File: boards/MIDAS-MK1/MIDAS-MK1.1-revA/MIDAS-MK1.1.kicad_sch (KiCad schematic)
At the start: 105 parts, among them J101 Left, J102 Right, J106 USB4105-GF-A, J107 DM3BT-DSF-PEJS, J108 Conn_01x02, J110 2157601003, J111 2157601003, SW101 SW_Push, SW102 SW_Push, U101 TCAL9539-Q1, U102 TCAL9539-Q1, U103 TCAL9539-Q1, U104 ESP32-S3-WROOM-1U, U105 MCP2518FDT-xSL, U106 MTFCxxxx, U107 TCAN337G, U108 ADS7138-Q1, U109 ECMF02-2AMX6, Y101 40MHz

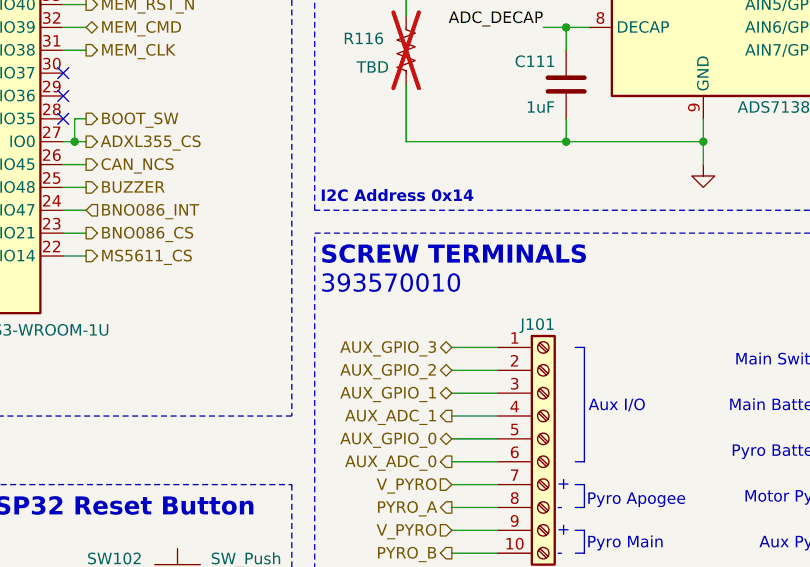
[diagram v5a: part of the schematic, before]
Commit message: rerouted regulator, added correct terminal block MPN to sch
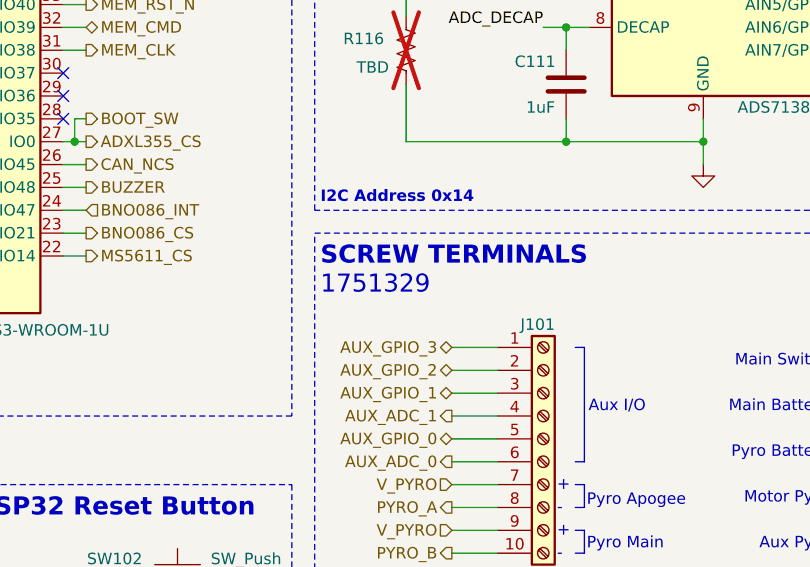
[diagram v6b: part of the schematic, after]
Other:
- note added: "1751329"
- note removed: "393570010"
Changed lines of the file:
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@@
     (effects (font (size 1.27 1.27) italic) (justify left bottom))
   )
-  (text "393570010" (at 175.895 235.585 0)
+  (text "1751329" (at 175.895 235.585 0)
     (effects (font (size 2 2)) (justify left bottom))
   )

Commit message: finalized SMA, renamed expander symbols, added backside labels, changed SYS_POWER test point, changed microSD 3D model color, other small stuff
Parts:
- U101, U102, U103: symbol Expander_Texas:TCAL9539-Q1 -> Interface_Expander_Texas:TCAL9539-Q1
- U108: symbol ADC_Texas:ADS7138-Q1 -> Analog_ADC_Texas:ADS7138-Q1
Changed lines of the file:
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@@
     )
   )
-  (symbol (lib_id "Expander_Texas:TCAL9539-Q1") (at 48.26 132.08 0) (unit 1)
+  (symbol (lib_id "Interface_Expander_Texas:TCAL9539-Q1") (at 48.26 132.08 0) (unit 1)
     (in_bom yes) (on_board yes) (dnp no)
     (property "Reference" "U102" (at 38.1 107.95 0)
@@
       (effects (font (size 1.27 1.27)) (justify left))
     )
-    (property "Footprint" "Package_DFN_QFN:WQFN-24-1EP_4x4mm_P0.5mm_EP2.6x2.6mm" (at 48.26 132.08 0)
-      (effects (font (size 1.27 1.27)) hide)
-    )
-    (property "Datasheet" "https://www.ti.com/lit/ds/symlink/tcal9539-q1.pdf" (at 48.26 132.08 0)
+    (property "Footprint" "Package_DFN_QFN:WQFN-24-1EP_4x4mm_P0.5mm_EP2.6x2.6mm" (at 48.26 162.56 0)
+      (effects (font (size 1.27 1.27)) hide)
+    )
+    (property "Datasheet" "https://www.ti.com/lit/ds/symlink/tcal9539-q1.pdf" (at 48.26 165.1 0)
       (effects (font (size 1.27 1.27)) hide)
     )
@@
     )
   )
-  (symbol (lib_name "TCAL9539-Q1_1") (lib_id "Expander_Texas:TCAL9539-Q1") (at 48.26 53.34 0) (unit 1)
+  (symbol (lib_id "Interface_Expander_Texas:TCAL9539-Q1") (at 48.26 53.34 0) (unit 1)
     (in_bom yes) (on_board yes) (dnp no)
     (property "Reference" "U101" (at 38.1 29.21 0)
@@
       (effects (font (size 1.27 1.27)) (justify left))
     )
-    (property "Footprint" "Package_DFN_QFN:WQFN-24-1EP_4x4mm_P0.5mm_EP2.6x2.6mm" (at 48.26 53.34 0)
-      (effects (font (size 1.27 1.27)) hide)
-    )
-    (property "Datasheet" "https://www.ti.com/lit/ds/symlink/tcal9539-q1.pdf" (at 48.26 53.34 0)
+    (property "Footprint" "Package_DFN_QFN:WQFN-24-1EP_4x4mm_P0.5mm_EP2.6x2.6mm" (at 48.26 83.82 0)
+      (effects (font (size 1.27 1.27)) hide)
+    )
+    (property "Datasheet" "https://www.ti.com/lit/ds/symlink/tcal9539-q1.pdf" (at 48.26 86.36 0)
       (effects (font (size 1.27 1.27)) hide)
     )
@@
     )
   )
-  (symbol (lib_id "ADC_Texas:ADS7138-Q1") (at 220.98 198.12 0) (unit 1)
+  (symbol (lib_id "Analog_ADC_Texas:ADS7138-Q1") (at 220.98 198.12 0) (unit 1)
     (in_bom yes) (on_board yes) (dnp no)
     (property "Reference" "U108" (at 208.28 184.15 0)
@@
       (effects (font (size 1.27 1.27)) (justify left))
     )
-    (property "Footprint" "Package_DFN_QFN:WQFN-16-1EP_3x3mm_P0.5mm_EP1.68x1.68mm" (at 220.98 198.12 0)
-      (effects (font (size 1.27 1.27)) hide)
-    )
-    (property "Datasheet" "https://www.ti.com/lit/ds/symlink/ads7138-q1.pdf" (at 220.98 198.12 0)
+    (property "Footprint" "Package_DFN_QFN:WQFN-16-1EP_3x3mm_P0.5mm_EP1.68x1.68mm" (at 220.98 218.44 0)
+      (effects (font (size 1.27 1.27)) hide)
+    )
+    (property "Datasheet" "https://www.ti.com/lit/ds/symlink/ads7138-q1.pdf" (at 220.98 220.98 0)
       (effects (font (size 1.27 1.27)) hide)
     )
@@
     )
   )
-  (symbol (lib_id "Expander_Texas:TCAL9539-Q1") (at 48.26 210.82 0) (unit 1)
+  (symbol (lib_id "Interface_Expander_Texas:TCAL9539-Q1") (at 48.26 210.82 0) (unit 1)
     (in_bom yes) (on_board yes) (dnp no)
     (property "Reference" "U103" (at 38.1 186.69 0)
@@
       (effects (font (size 1.27 1.27)) (justify left))
     )
-    (property "Footprint" "Package_DFN_QFN:WQFN-24-1EP_4x4mm_P0.5mm_EP2.6x2.6mm" (at 48.26 210.82 0)
-      (effects (font (size 1.27 1.27)) hide)
-    )
-    (property "Datasheet" "https://www.ti.com/lit/ds/symlink/tcal9539-q1.pdf" (at 48.26 210.82 0)
-      (effects (font (size 1.27 1.27)) hide)
-    )
+    (property "Footprint" "Package_DFN_QFN:WQFN-24-1EP_4x4mm_P0.5mm_EP2.6x2.6mm" (at 48.26 241.3 0)
+      (effects (font (size 1.27 1.27)) hide)
+    )
+    (property "Datasheet" "https://www.ti.com/lit/ds/symlink/tcal9539-q1.pdf" (at 48.26 243.84 0)
+      (effects (font (size 1.27 1.27)) hide)
+    )

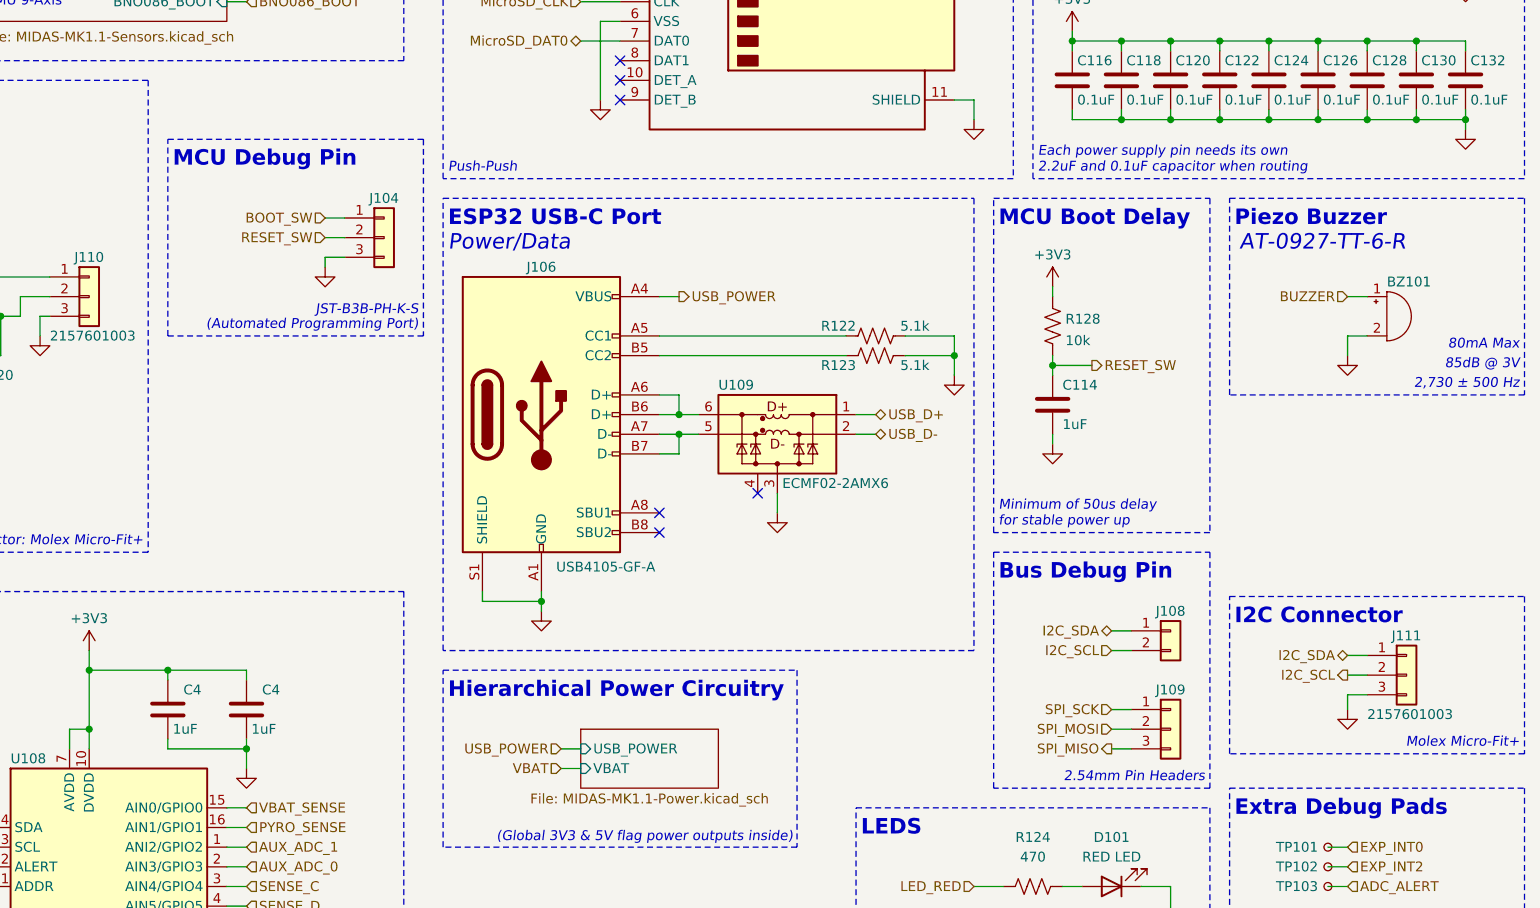
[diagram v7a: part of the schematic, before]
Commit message: schematic organizational changes
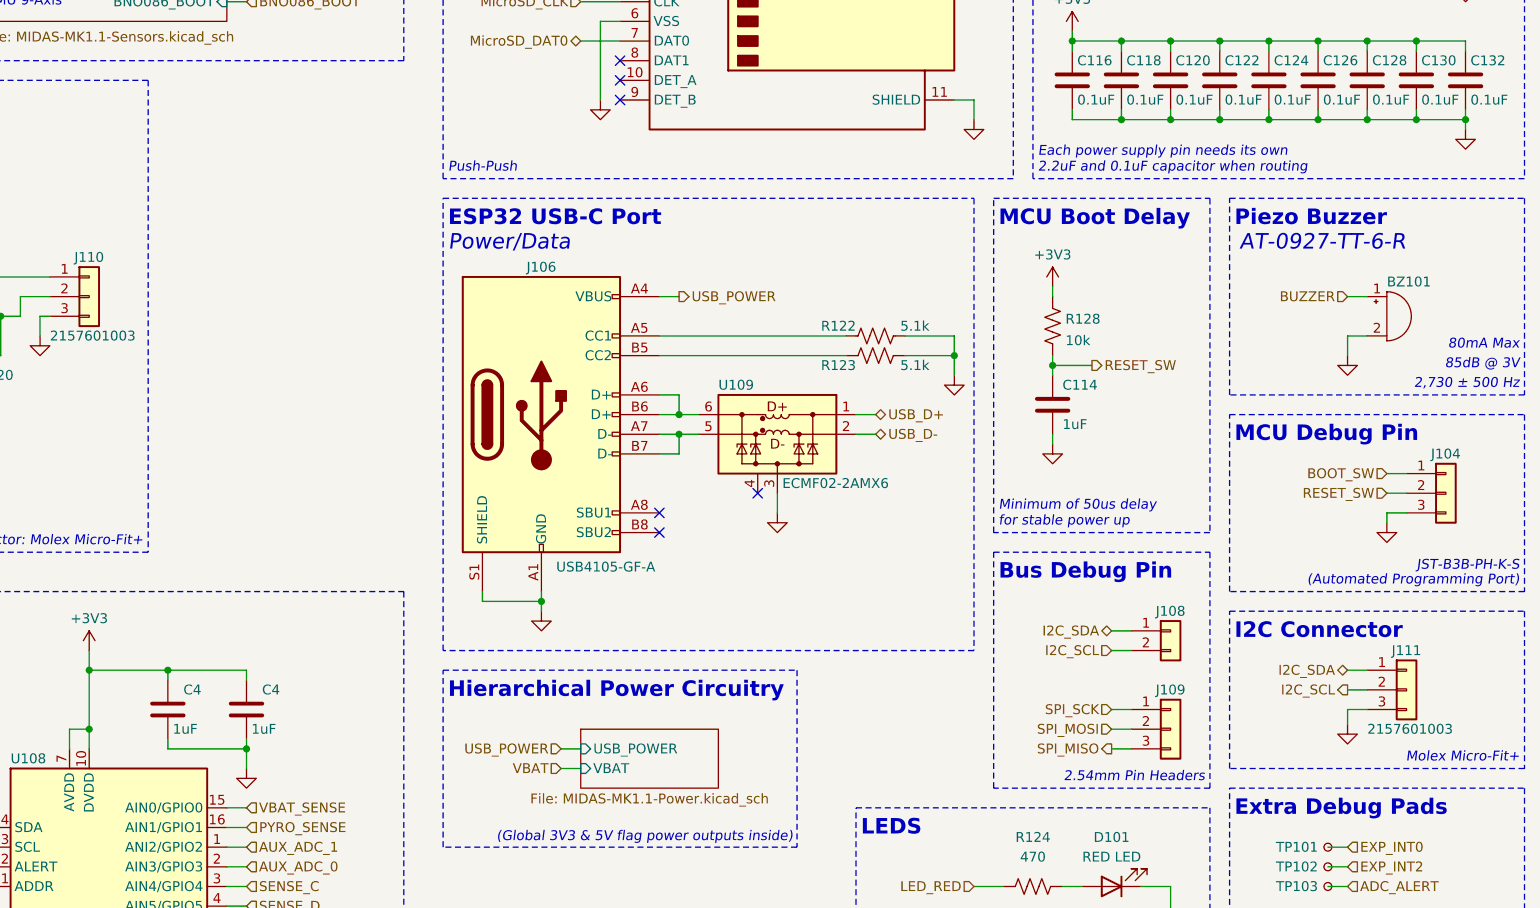
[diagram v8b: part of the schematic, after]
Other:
- moved on the sheet: J104, J111
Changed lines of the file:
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@@
     (stroke (width 0) (type default))
   )
-  (wire (pts (xy 248.92 114.3) (xy 251.46 114.3))
+  (wire (pts (xy 386.08 147.32) (xy 388.62 147.32))
     (stroke (width 0) (type default))
   )
@@
     (stroke (width 0) (type default))
   )
-  (wire (pts (xy 381 175.895) (xy 383.54 175.895))
+  (wire (pts (xy 381 177.8) (xy 383.54 177.8))
     (stroke (width 0) (type default))
   )
@@
     (stroke (width 0) (type default))
   )
-  (wire (pts (xy 381 175.895) (xy 381 177.8))
+  (wire (pts (xy 381 177.8) (xy 381 179.705))
     (stroke (width 0) (type default))
   )
@@
     (stroke (width 0) (type default))
   )
-  (wire (pts (xy 381 170.815) (xy 383.54 170.815))
+  (wire (pts (xy 381 172.72) (xy 383.54 172.72))
     (stroke (width 0) (type default))
   )
@@
     (stroke (width 0) (type default))
   )
-  (wire (pts (xy 381 173.355) (xy 383.54 173.355))
+  (wire (pts (xy 381 175.26) (xy 383.54 175.26))
     (stroke (width 0) (type default))
   )
@@
     (stroke (width 0) (type default))
   )
-  (wire (pts (xy 248.92 119.38) (xy 248.92 120.65))
+  (wire (pts (xy 386.08 152.4) (xy 386.08 153.67))
     (stroke (width 0) (type default))
   )
@@
     (stroke (width 0) (type default))
   )
-  (wire (pts (xy 248.92 116.84) (xy 251.46 116.84))
+  (wire (pts (xy 386.08 149.86) (xy 388.62 149.86))
     (stroke (width 0) (type default))
   )
@@
     (stroke (width 0) (type default))
   )
-  (wire (pts (xy 251.46 119.38) (xy 248.92 119.38))
+  (wire (pts (xy 388.62 152.4) (xy 386.08 152.4))
     (stroke (width 0) (type default))
   )
@@
     (stroke (width 0) (type default))
   )
-  (rectangle (start 228.6 104.14) (end 261.62 129.54)
+  (rectangle (start 365.76 139.7) (end 403.86 162.56)
     (stroke (width 0) (type dash))
     (fill (type none))
@@
     (fill (type none))
   )
-  (rectangle (start 365.76 163.195) (end 403.86 183.515)
+  (rectangle (start 365.76 165.1) (end 403.86 185.42)
     (stroke (width 0) (type dash))
     (fill (type none))
@@
     (effects (font (size 1.27 1.27) italic) (justify left bottom))
   )
-  (text "MCU Debug Pin\n\n" (at 229.235 111.125 0)
+  (text "MCU Debug Pin\n\n" (at 366.395 146.685 0)
     (effects (font (size 2 2) (thickness 0.4) bold) (justify left bottom))
   )
@@
     (effects (font (size 2 2) (thickness 0.4) bold) (justify left bottom))
   )
-  (text "(Automated Programming Port)" (at 260.985 128.905 0)
+  (text "(Automated Programming Port)" (at 403.225 161.925 0)
     (effects (font (size 1.27 1.27) italic) (justify right bottom))
   )
@@
     (effects (font (size 1.27 1.27)) (justify left bottom))
   )
-  (text "Molex Micro-Fit+" (at 403.225 182.88 0)
+  (text "Molex Micro-Fit+" (at 403.225 184.785 0)
     (effects (font (size 1.27 1.27) italic) (justify right bottom))
   )
@@
     (effects (font (size 1.27 1.27)) (justify left bottom))
   )
-  (text "JST-B3B-PH-K-S" (at 260.985 127 0)
+  (text "JST-B3B-PH-K-S" (at 403.225 160.02 0)
     (effects (font (size 1.27 1.27) italic) (justify right bottom))
   )
@@
     (effects (font (size 1.27 1.27)) (justify left bottom))
   )
-  (text "I2C Connector\n" (at 366.395 167.005 0)
+  (text "I2C Connector\n" (at 366.395 168.91 0)
     (effects (font (size 2 2) (thickness 0.4) bold) (justify left bottom))
   )
@@
     (effects (font (size 1.27 1.27)) (justify left))
   )
-  (hierarchical_label "I2C_SDA" (shape bidirectional) (at 381 170.815 180) (fields_autoplaced)
+  (hierarchical_label "I2C_SDA" (shape bidirectional) (at 381 172.72 180) (fields_autoplaced)
     (effects (font (size 1.27 1.27)) (justify right))
   )
@@
     (effects (font (size 1.27 1.27)) (justify right))
   )
-  (hierarchical_label "RESET_SW" (shape input) (at 248.92 116.84 180) (fields_autoplaced)
+  (hierarchical_label "RESET_SW" (shape input) (at 386.08 149.86 180) (fields_autoplaced)
     (effects (font (size 1.27 1.27)) (justify right))
   )
@@
     (effects (font (size 1.27 1.27)) (justify left))
   )
-  (hierarchical_label "I2C_SCL" (shape output) (at 381 173.355 180) (fields_autoplaced)
+  (hierarchical_label "I2C_SCL" (shape output) (at 381 175.26 180) (fields_autoplaced)
     (effects (font (size 1.27 1.27)) (justify right))
   )
@@
     (effects (font (size 1.27 1.27)) (justify right))
   )
-  (hierarchical_label "BOOT_SW" (shape input) (at 248.92 114.3 180) (fields_autoplaced)
+  (hierarchical_label "BOOT_SW" (shape input) (at 386.08 147.32 180) (fields_autoplaced)
     (effects (font (size 1.27 1.27)) (justify right))
   )
@@
     )
   )
-  (symbol (lib_id "Connector_Generic:Conn_01x03") (at 388.62 173.355 0) (unit 1)
+  (symbol (lib_id "Connector_Generic:Conn_01x03") (at 388.62 175.26 0) (unit 1)
     (in_bom yes) (on_board yes) (dnp no)
-    (property "Reference" "J111" (at 388.62 168.275 0)
+    (property "Reference" "J111" (at 388.62 170.18 0)
       (effects (font (size 1.27 1.27)))
     )
-    (property "Value" "2157601003" (at 383.54 178.435 0)
+    (property "Value" "2157601003" (at 383.54 180.34 0)
       (effects (font (size 1.27 1.27)) (justify left))
     )
-    (property "Footprint" "Connector_Molex_Micro-Fit-Plus:Molex_Micro-Fit-Plus_2157601003_1x03_P3.0mm" (at 388.62 173.355 0)
+    (property "Footprint" "Connector_Molex_Micro-Fit-Plus:Molex_Micro-Fit-Plus_2157601003_1x03_P3.0mm" (at 388.62 175.26 0)
       (effects (font (size 1.27 1.27)) hide)
     )
-    (property "Datasheet" "~" (at 388.62 173.355 0)
+    (property "Datasheet" "~" (at 388.62 175.26 0)
       (effects (font (size 1.27 1.27)) hide)
     )
@@
     )
   )
-  (symbol (lib_id "power:GND") (at 248.92 120.65 0) (unit 1)
+  (symbol (lib_id "power:GND") (at 386.08 153.67 0) (unit 1)
     (in_bom yes) (on_board yes) (dnp no) (fields_autoplaced)
-    (property "Reference" "#PWR0137" (at 248.92 127 0)
+    (property "Reference" "#PWR0137" (at 386.08 160.02 0)
       (effects (font (size 1.27 1.27)) hide)
     )
-    (property "Value" "GND" (at 248.92 125.095 0)
+    (property "Value" "GND" (at 386.08 158.115 0)
       (effects (font (size 1.27 1.27)) hide)
     )
-    (property "Footprint" "" (at 248.92 120.65 0)
+    (property "Footprint" "" (at 386.08 153.67 0)
       (effects (font (size 1.27 1.27)) hide)
     )
-    (property "Datasheet" "" (at 248.92 120.65 0)
+    (property "Datasheet" "" (at 386.08 153.67 0)
       (effects (font (size 1.27 1.27)) hide)
     )
@@
     )
   )
-  (symbol (lib_id "power:GND") (at 381 177.8 0) (unit 1)
+  (symbol (lib_id "power:GND") (at 381 179.705 0) (unit 1)
     (in_bom yes) (on_board yes) (dnp no) (fields_autoplaced)
-    (property "Reference" "#PWR0155" (at 381 184.15 0)
+    (property "Reference" "#PWR0155" (at 381 186.055 0)
       (effects (font (size 1.27 1.27)) hide)
     )
-    (property "Value" "GND" (at 381 182.245 0)
+    (property "Value" "GND" (at 381 184.15 0)
       (effects (font (size 1.27 1.27)) hide)
     )
-    (property "Footprint" "" (at 381 177.8 0)
+    (property "Footprint" "" (at 381 179.705 0)
       (effects (font (size 1.27 1.27)) hide)
     )
-    (property "Datasheet" "" (at 381 177.8 0)
+    (property "Datasheet" "" (at 381 179.705 0)
       (effects (font (size 1.27 1.27)) hide)
     )
@@
     )
   )
-  (symbol (lib_id "Connector_Generic:Conn_01x03") (at 256.54 116.84 0) (unit 1)
+  (symbol (lib_id "Connector_Generic:Conn_01x03") (at 393.7 149.86 0) (unit 1)
     (in_bom yes) (on_board yes) (dnp no)
-    (property "Reference" "J104" (at 256.54 111.76 0)
+    (property "Reference" "J104" (at 393.7 144.78 0)
       (effects (font (size 1.27 1.27)))
     )
-    (property "Value" "~" (at 259.08 118.11 0)
+    (property "Value" "~" (at 396.24 151.13 0)
       (effects (font (size 1.27 1.27)) (justify left) hide)
     )
-    (property "Footprint" "Connector_JST:JST_PH_B3B-PH-K_1x03_P2.00mm_Vertical" (at 256.54 116.84 0)
+    (property "Footprint" "Connector_JST:JST_PH_B3B-PH-K_1x03_P2.00mm_Vertical" (at 393.7 149.86 0)
       (effects (font (size 1.27 1.27)) hide)
     )
-    (property "Datasheet" "~" (at 256.54 116.84 0)
+    (property "Datasheet" "~" (at 393.7 149.86 0)
       (effects (font (size 1.27 1.27)) hide)
     )
